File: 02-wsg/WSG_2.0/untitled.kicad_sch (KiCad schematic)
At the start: 22 parts, among them IC1 W25N04KVZEIR, IC5 AP2120N-3.3TRG1, IC8 SPX3819S-L_TR, J1 USB4110-GF-A, J4 Conn_01x02

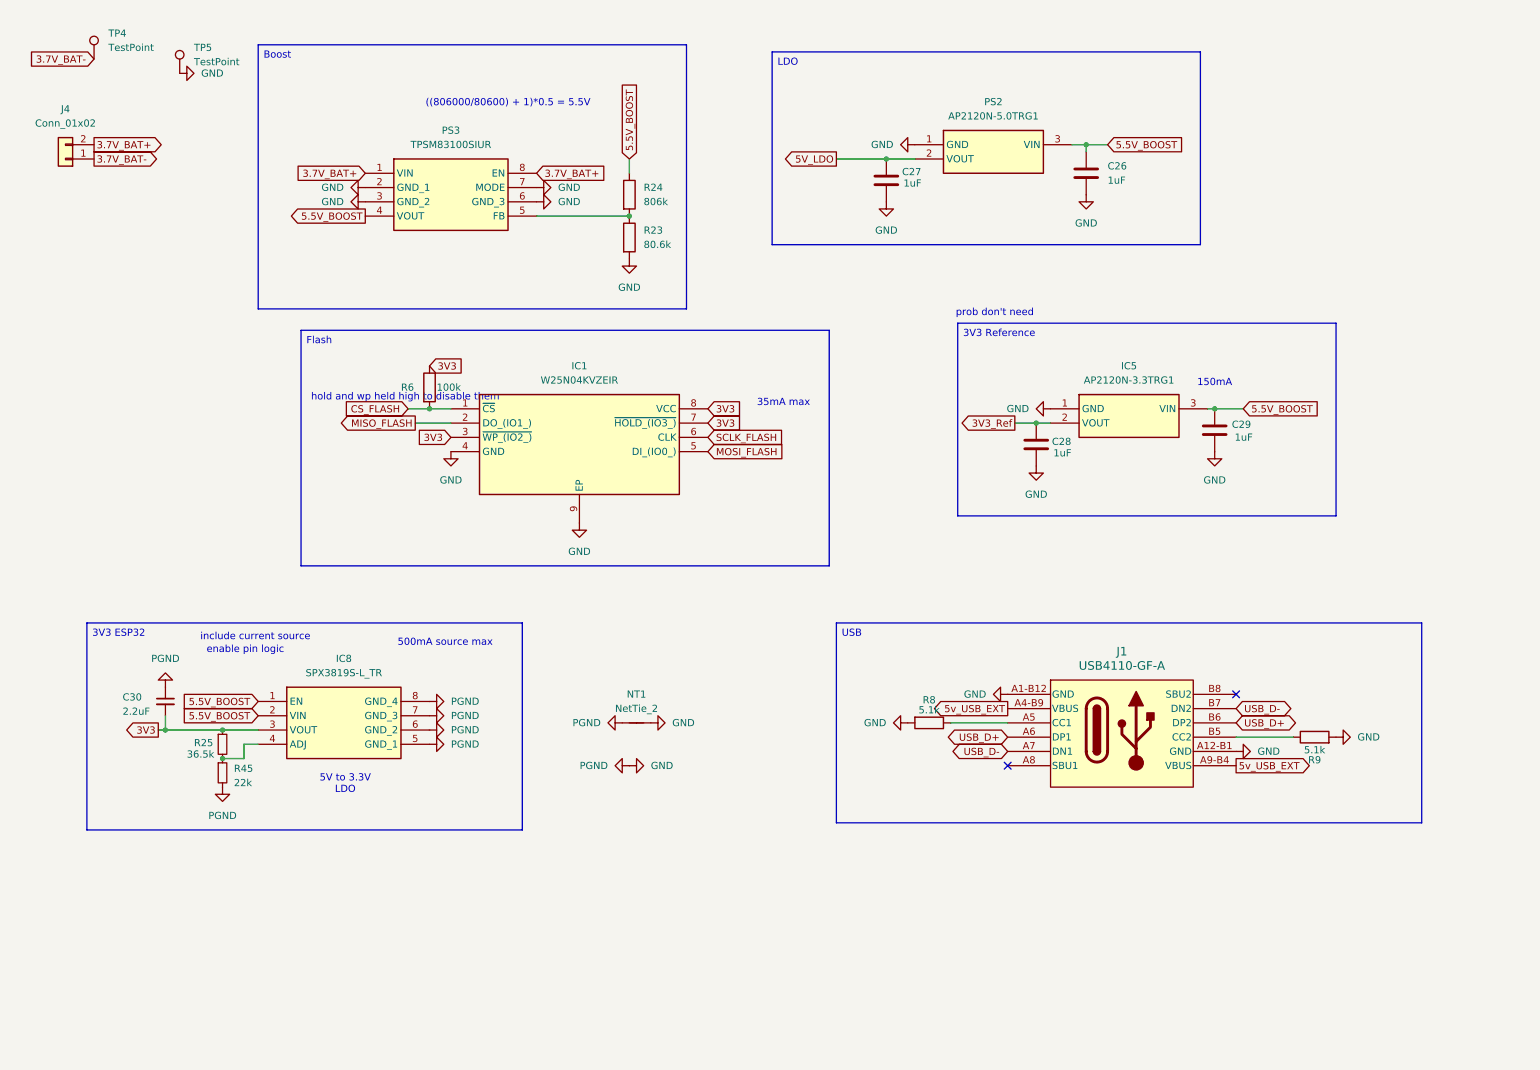
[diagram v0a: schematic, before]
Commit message: Added lithium charger and fixed unconnected items
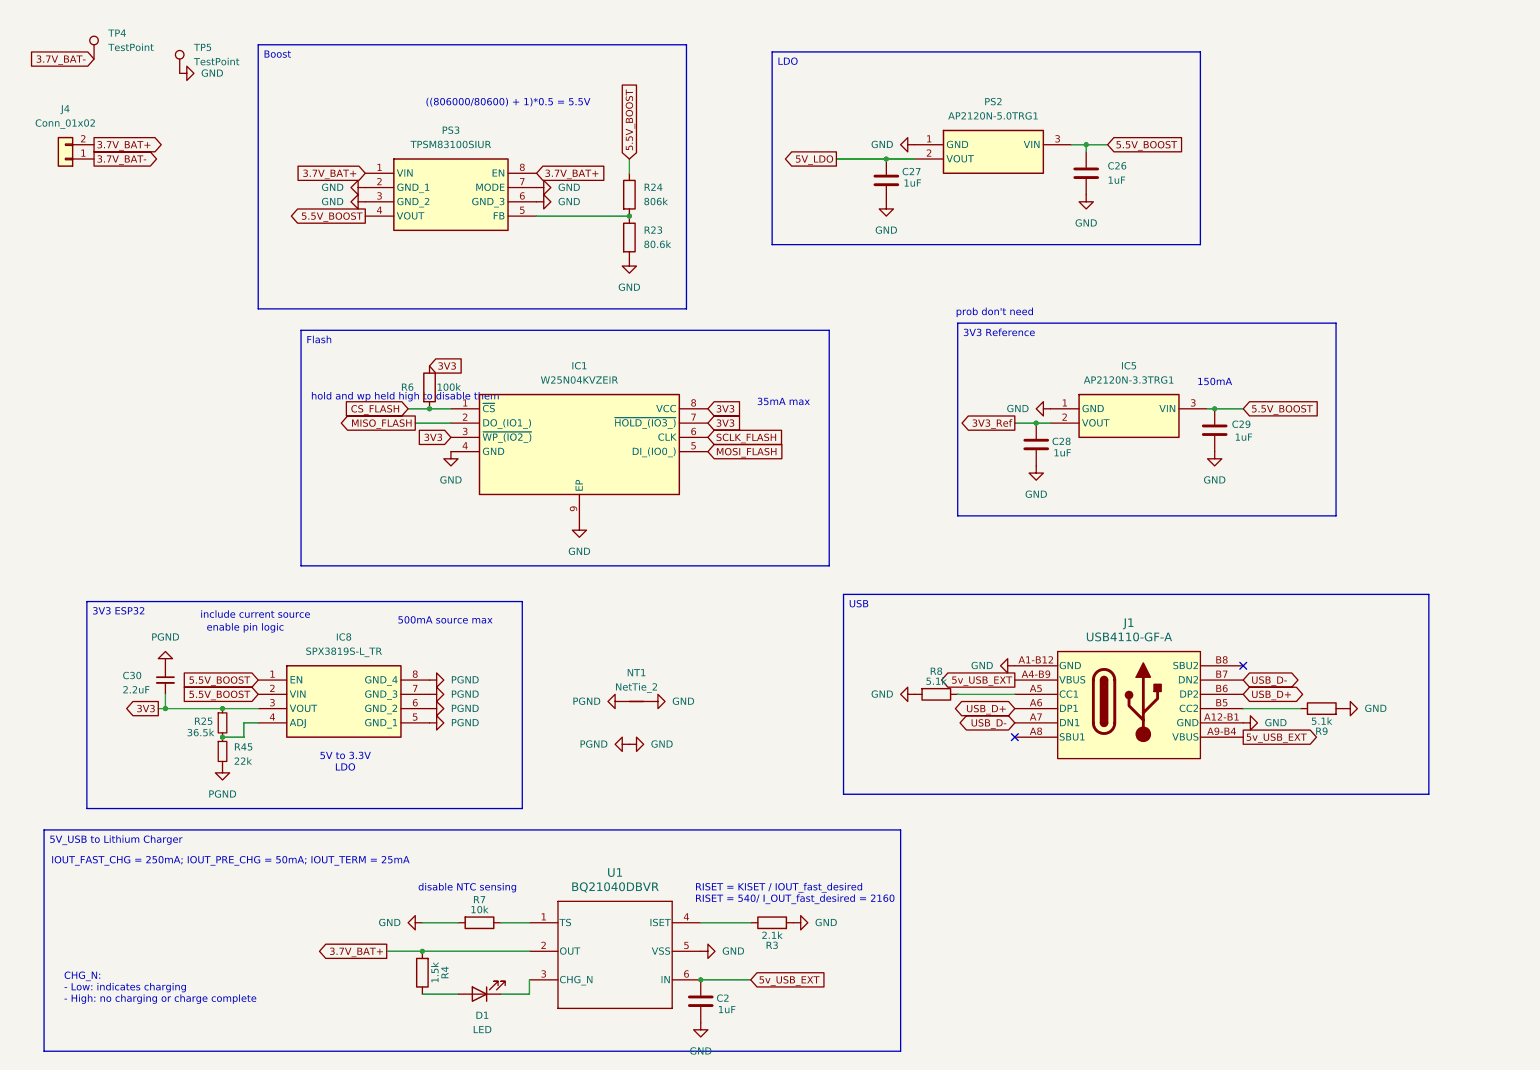
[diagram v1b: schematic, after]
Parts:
- added C2: 1uF, Capacitor_SMD:C_0603_1608Metric, symbol Device:C
- added D1: LED, Diode_SMD:D_0402_1005Metric, symbol Device:LED
- added R3: 2.1k, Resistor_SMD:R_0402_1005Metric, symbol Device:R
- added R4: 1.5k, Resistor_SMD:R_0402_1005Metric, symbol Device:R
- added R7: 10k, Resistor_SMD:R_0402_1005Metric, symbol Device:R
- added U1: BQ21040DBVR, 22XT_WSG_Rev1:BQ21040DBVR, symbol 22XT_WSG_Rev1:BQ21040DBVR
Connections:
- net 3.7V_BAT+: now also R4.2, U1.2 (OUT)
- net 5v_USB_EXT: now also C2.1, U1.6 (IN)
- net GND: now also C2.2, R3.2, R7.2, U1.5 (VSS)
- new net: D1.2 (A), R4.1
- new net: R7.1, U1.1 (TS)
- new net: D1.1 (K), U1.3 (CHG_N)
- new net: R3.1, U1.4 (ISET)
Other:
- note added: "CHG_N: - Low: indicates charging - High: no charging or charge complete"
- note added: "IOUT_FAST_CHG = 250mA; IOUT_PRE_CHG = 50mA; IOUT_TERM = 25mA"
- note added: "RISET = KISET / IOUT_fast_desired RISET = 540/ I_OUT_fast_desired = 2160"
- note added: "disable NTC sensing"
- moved on the sheet: C30, IC8, J1, NT1, R25, R45, R8, R9

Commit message: layout and schematic updates
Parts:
- added C11: 47uF, Capacitor_SMD:C_0402_1005Metric, symbol Device:C
- added C12: 22uF, Capacitor_SMD:C_0402_1005Metric, symbol Device:C
- added R2, R28: 22R, Resistor_SMD:R_0402_1005Metric, symbol Device:R
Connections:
- net 3.7V_BAT+: now also C12.2
- net 5.5V_BOOST: now also C11.1
- net GND: now also C11.2, C12.1
- net USB_D+: now also R28.1
- net USB_D-: now also R2.1
- new net ESP_USB_D+: R2.2
- new net ESP_USB_D-: R28.2
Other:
- moved on the sheet: C30, R8, TP5

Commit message: ready for review
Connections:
- net ESP_USB_D+: now also R28.2; no longer R2.2
- net ESP_USB_D-: now also R2.2; no longer R28.2
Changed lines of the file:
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@@
 		)
 	)
-	(global_label "ESP_USB_D-"
+	(global_label "ESP_USB_D+"
 		(shape bidirectional)
 		(at 259.08 130.81 0)
@@
 		)
 	)
-	(global_label "ESP_USB_D+"
+	(global_label "ESP_USB_D-"
 		(shape bidirectional)
 		(at 259.08 125.73 0)

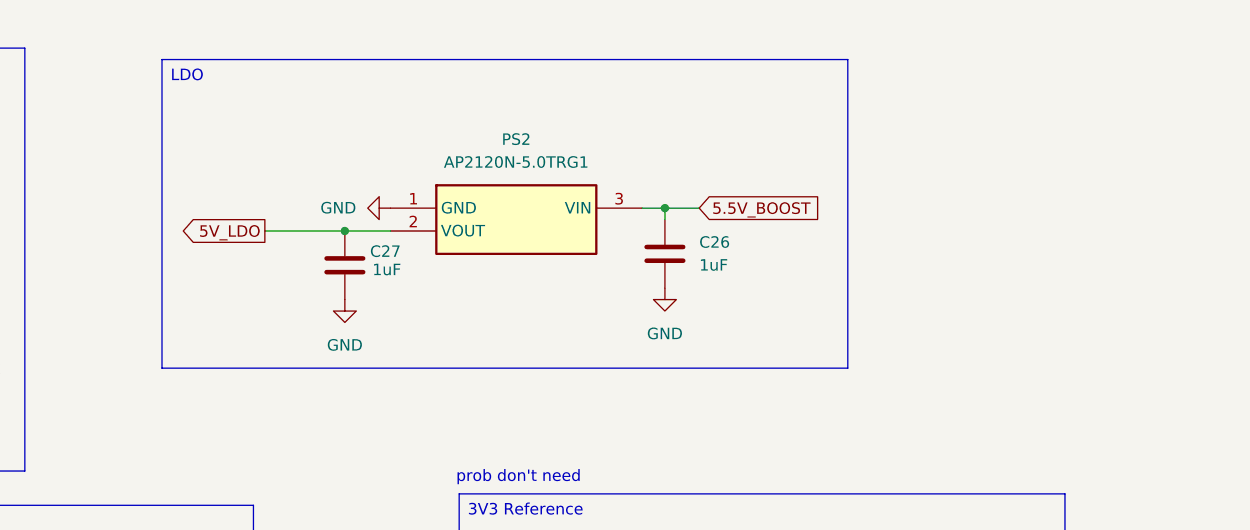
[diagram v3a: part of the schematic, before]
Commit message: added reg
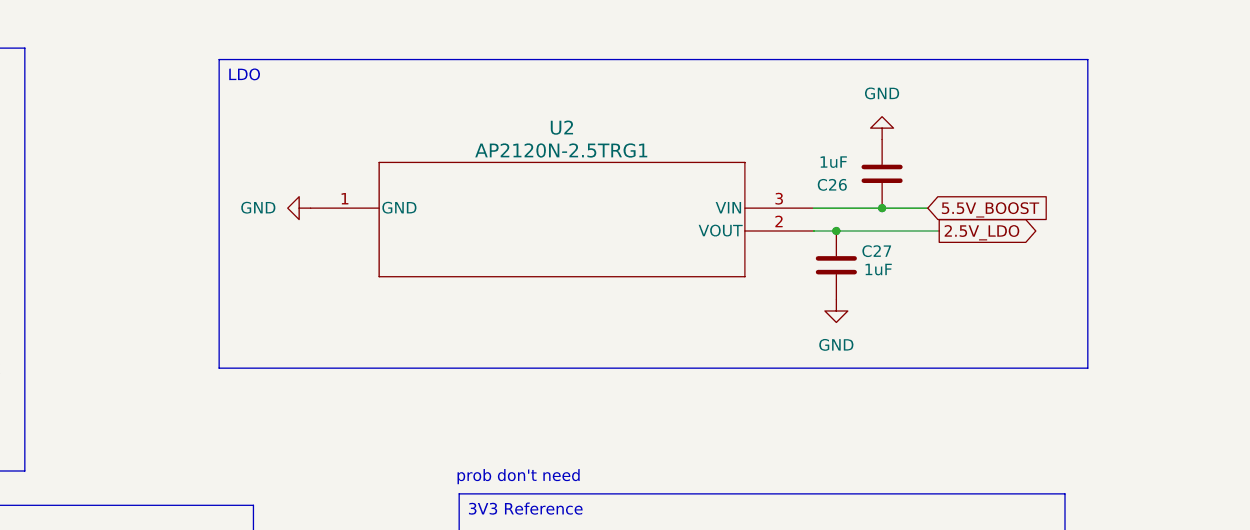
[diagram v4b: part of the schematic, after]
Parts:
- removed PS2: AP2120N-5.0TRG1, wsg_fp:AP2120N-5.0TRG, symbol 22xt_ICs:AP2120N-5.0TRG1
- added U2: AP2120N-2.5TRG1, 22xt_wsg_footprints:2.5_LDO, symbol 22xt_ICs:AP2120N-2.5TRG1
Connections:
- net 5.5V_BOOST: now also U2.3 (VIN)
- net GND: now also U2.1 (GND)
- net 5V_LDO renamed 2.5V_LDO
- net 2.5V_LDO: now also U2.2 (VOUT)
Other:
- moved on the sheet: C26, C27

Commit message: layout
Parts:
- removed C26, C27: 1uF, Capacitor_SMD:C_0402_1005Metric, symbol Device:C
- removed IC5: AP2120N-3.3TRG1, wsg_fp:AP2120N-3.3TRG1, symbol 22xt_ICs:AP2120N-3.3TRG1
- removed U2: AP2120N-2.5TRG1, 22xt_wsg_footprints:2.5_LDO, symbol 22xt_ICs:AP2120N-2.5TRG1
- added C13: 1uF, Capacitor_SMD:C_0402_1005Metric, symbol Device:C
- added C14: 0.1uF, Capacitor_SMD:C_0402_1005Metric, symbol Device:C
- added D2: D, 22xt_wsg_footprints:DIO_RB161QS_ROM(diode), symbol Device:D
- added IC3: MIC5504-3.3YM5-TR, 22xt_wsg_footprints:MIC5501234 (3.3v ref), symbol 22xt_ICs:MIC5504-3.3YM5-TR
- added MOSFET1: DMP2120U-7, 22xt_wsg_footprints:SOT-23_DMP2120U_DIO-L, symbol 22xt_ICs:DMP2120U-7
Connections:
- net 3V3_Ref: now also IC3.5 (VOUT)
- net 5.5V_BOOST: now also IC3.1 (VIN), IC3.3 (EN), MOSFET1.2 (S); no longer IC8.1 (EN), IC8.2 (VIN)
- net 5v_USB_EXT: now also C13.1, C14.1, D2.2 (A), MOSFET1.1 (G)
- net GND: now also C13.2, C14.2, IC3.2 (GND)
- new net VIN: D2.1 (K), IC8.1 (EN), IC8.2 (VIN), MOSFET1.3 (D)
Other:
- note added: "300mA"
- note added: "V_TH = -1V"
- note added: "V_fwd = 300 mV at 500 mA"
- note added: "|V_DS| < |V_GS -V_TH| for triode |4.7| < |0-5.5+1|"
- note removed: "150mA"
- note removed: "prob don't need"
- moved on the sheet: C11, C12, C28, C29, C30, IC1, IC8, J1, J4, NT1, PS3, R2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

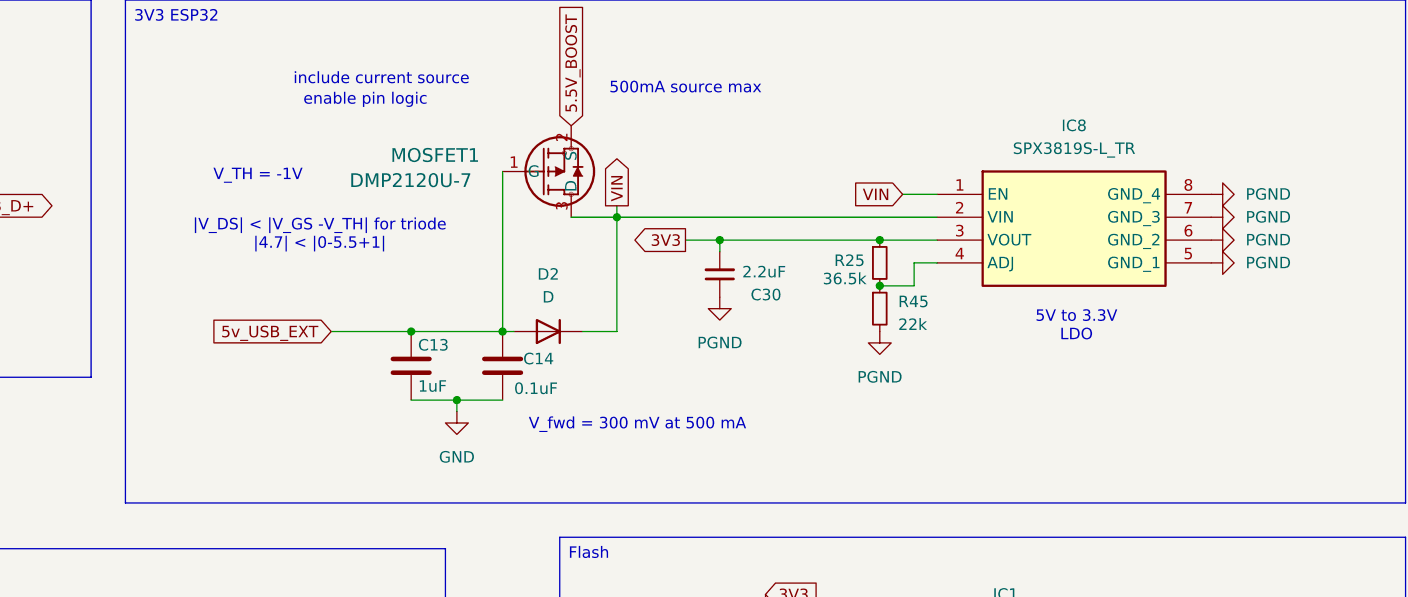
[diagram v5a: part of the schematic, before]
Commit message: Edited on-circuit 3v3 ldo
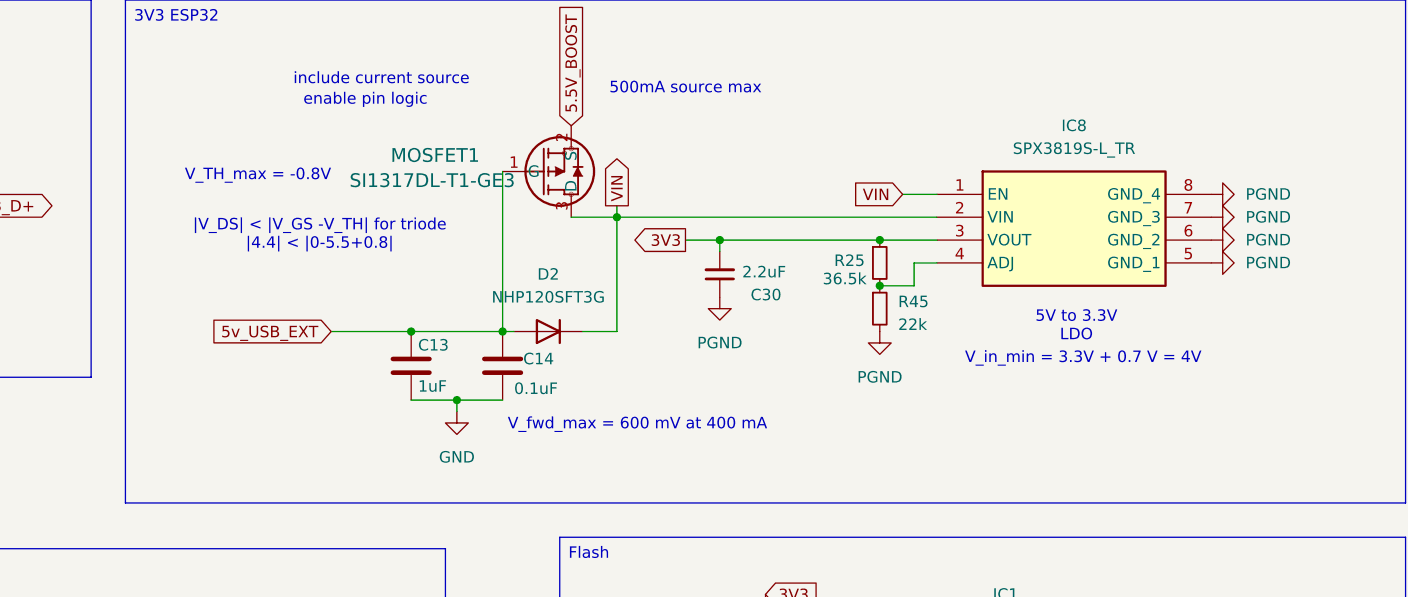
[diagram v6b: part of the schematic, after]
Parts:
- D2: value D -> NHP120SFT3G; footprint 22xt_wsg_footprints:DIO_RB161QS_ROM(diode) -> Diode_SMD:D_SOD-123F
- MOSFET1: value DMP2120U-7 -> SI1317DL-T1-GE3
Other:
- note added: "V_TH_max = -0.8V"
- note added: "V_fwd_max = 600 mV at 400 mA"
- note added: "V_in_min = 3.3V + 0.7 V = 4V"
- note added: "|V_DS| < |V_GS -V_TH| for triode |4.4| < |0-5.5+0.8|"
- note removed: "V_TH = -1V"
- note removed: "V_fwd = 300 mV at 500 mA"
- note removed: "|V_DS| < |V_GS -V_TH| for triode |4.7| < |0-5.5+1|"
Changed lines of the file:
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@@
 		)
 	)
-	(text "|V_DS| < |V_GS -V_TH| for triode\n|4.7| < |0-5.5+1|"
+	(text "V_in_min = 3.3V + 0.7 V = 4V"
+		(exclude_from_sim no)
+		(at 244.856 52.578 0)
+		(effects
+			(font
+				(size 1.27 1.27)
+			)
+		)
+	)
+	(text "|V_DS| < |V_GS -V_TH| for triode\n|4.4| < |0-5.5+0.8|"
 		(exclude_from_sim no)
 		(at 160.02 38.862 0)
@@
 		)
 	)
-	(text "V_fwd = 300 mV at 500 mA"
+	(text "V_fwd_max = 600 mV at 400 mA"
 		(exclude_from_sim no)
 		(at 195.326 59.944 0)
@@
 		)
 	)
-	(text "V_TH = -1V"
+	(text "V_TH_max = -0.8V"
 		(exclude_from_sim no)
 		(at 153.162 32.258 0)
@@
 			)
 		)
-		(property "Value" "DMP2120U-7"
+		(property "Value" "SI1317DL-T1-GE3"
 			(at 163.322 32.766 0)
 			(effects
@@
 			)
 		)
-		(property "Value" "D"
+		(property "Value" "NHP120SFT3G"
 			(at 185.42 45.72 0)
 			(effects
@@
 			)
 		)
-		(property "Footprint" "22xt_wsg_footprints:DIO_RB161QS_ROM(diode)"
+		(property "Footprint" "Diode_SMD:D_SOD-123F"
 			(at 185.42 49.53 0)
 			(effects

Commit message: Edited comments/flag titles
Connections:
- net CS_FLASH renamed CS_NAND_FLASH
- net MISO_FLASH renamed MISO_NAND_FLASH
- net MOSI_FLASH renamed MOSI_NAND_FLASH
- net SCLK_FLASH renamed SCLK_NAND_FLASH
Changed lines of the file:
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@@
 		)
 	)
-	(text_box "Flash"
+	(text_box "NAND Flash: data storage"
 		(exclude_from_sim no)
 		(at 186.69 72.39 0)
@@
 		)
 	)
-	(text_box "5V_USB to Lithium Charger"
+	(text_box "5V_USB to Lithium Charger (3.7 V, 850 mAh): charging at 0.29 C"
 		(exclude_from_sim no)
 		(at 17.78 156.21 0)
@@
 		)
 	)
-	(global_label "CS_FLASH"
+	(global_label "CS_NAND_FLASH"
 		(shape input)
 		(at 205.74 86.36 180)
@@
 		)
 		(property "Intersheetrefs" "${INTERSHEET_REFS}"
-			(at 193.5624 86.36 0)
+			(at 187.5752 86.36 0)
 			(effects
 				(font
@@
 	(global_label "ESP_USB_D-"
 		(shape bidirectional)
-		(at 115.57 30.48 90)
-		(fields_autoplaced yes)
-		(effects
-			(font
-				(size 1.27 1.27)
-			)
-			(justify left)
-		)
-		(property "Intersheetrefs" "${INTERSHEET_REFS}"
-			(at 115.57 14.1674 90)
+		(at 115.57 30.48 0)
+		(fields_autoplaced yes)
+		(effects
+			(font
+				(size 1.27 1.27)
+			)
+			(justify left)
+		)
+		(property "Intersheetrefs" "${INTERSHEET_REFS}"
+			(at 131.8826 30.48 0)
 			(effects
 				(font
@@
 		)
 	)
-	(global_label "SCLK_FLASH"
+	(global_label "SCLK_NAND_FLASH"
 		(shape input)
 		(at 259.08 91.44 0)
@@
 		)
 		(property "Intersheetrefs" "${INTERSHEET_REFS}"
-			(at 273.5557 91.44 0)
+			(at 279.5429 91.44 0)
 			(effects
 				(font
@@
 		)
 	)
-	(global_label "MISO_FLASH"
+	(global_label "MISO_NAND_FLASH"
 		(shape output)
 		(at 207.01 88.9 180)
@@
 		)
 		(property "Intersheetrefs" "${INTERSHEET_REFS}"
-			(at 192.7157 88.9 0)
+			(at 186.7285 88.9 0)
 			(effects
 				(font
@@
 		)
 	)
-	(global_label "MOSI_FLASH"
+	(global_label "MOSI_NAND_FLASH"
 		(shape input)
 		(at 259.08 93.98 0)
@@
 		)
 		(property "Intersheetrefs" "${INTERSHEET_REFS}"
-			(at 273.3743 93.98 0)
-			(effects
-				(font
+			(at 279.3615 93.98 0)
+			(effects
+				(font

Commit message: layout done-still need to fix silkscreen-check antenna
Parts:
- MOSFET1: footprint 22xt_wsg_footprints:SOT-23_DMP2120U_DIO-L -> 22xt_wsg_footprints:SI1317DL-T1-GE3
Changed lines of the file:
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@@
 			)
 		)
-		(property "Footprint" "22xt_wsg_footprints:SOT-23_DMP2120U_DIO-L"
+		(property "Footprint" "22xt_wsg_footprints:SI1317DL-T1-GE3"
 			(at 180.34 31.75 0)
 			(effects
